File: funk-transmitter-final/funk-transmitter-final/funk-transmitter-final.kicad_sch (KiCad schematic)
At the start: 6 parts, among them J1 Conn_01x02_Socket, J2 Conn_01x08_Socket, J3 Conn_01x02_Socket, U1 Si4463_eigen

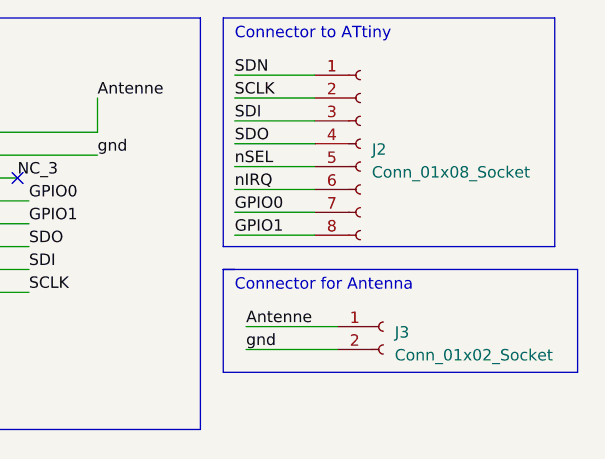
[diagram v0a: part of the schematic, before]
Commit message: display brain platine erweitert
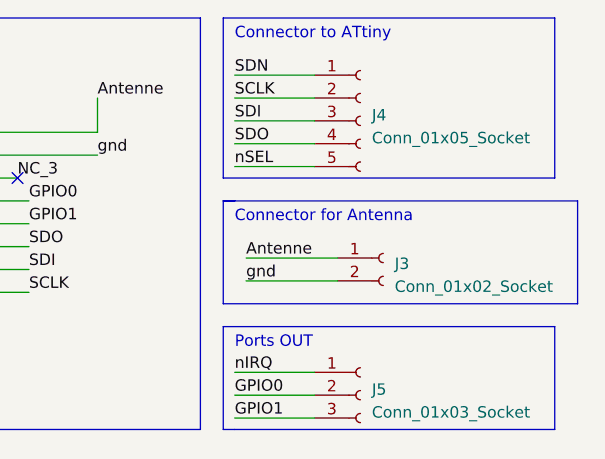
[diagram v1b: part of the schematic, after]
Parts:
- removed J2: Conn_01x08_Socket, Connector_PinHeader_2.54mm:PinHeader_1x08_P2.54mm_Vertical, symbol Connector:Conn_01x08_Socket
- added J4: Conn_01x05_Socket, Connector_PinHeader_2.54mm:PinHeader_1x05_P2.54mm_Vertical, symbol Connector:Conn_01x05_Socket
- added J5: Conn_01x03_Socket, Connector_PinSocket_2.54mm:PinSocket_1x03_P2.54mm_Vertical, symbol Connector:Conn_01x03_Socket
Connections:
- net GPIO0: now also J5.2 (Pin_2)
- net GPIO1: now also J5.3 (Pin_3)
- net SCLK: now also J4.2 (Pin_2)
- net SDI: now also J4.3 (Pin_3)
- net SDN: now also J4.1 (Pin_1)
- net SDO: now also J4.4 (Pin_4)
- net nIRQ: now also J5.1 (Pin_1)
- net nSEL: now also J4.5 (Pin_5)
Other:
- note added: "Ports OUT"
- moved on the sheet: J3
